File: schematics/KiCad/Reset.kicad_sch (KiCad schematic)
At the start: 15 parts, among them SW2 RESET, U13 74HC08, U14 74HC74, U14 DS1232, U15 DS1232, U2 74HC04, U9 74HC08, Y2 8MHz

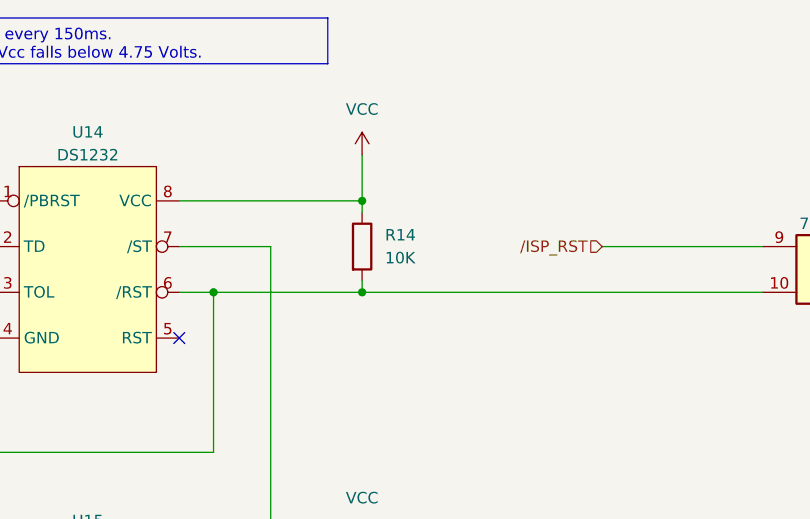
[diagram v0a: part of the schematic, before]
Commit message: Pull up ISP CLK by 10K ohm resistor.
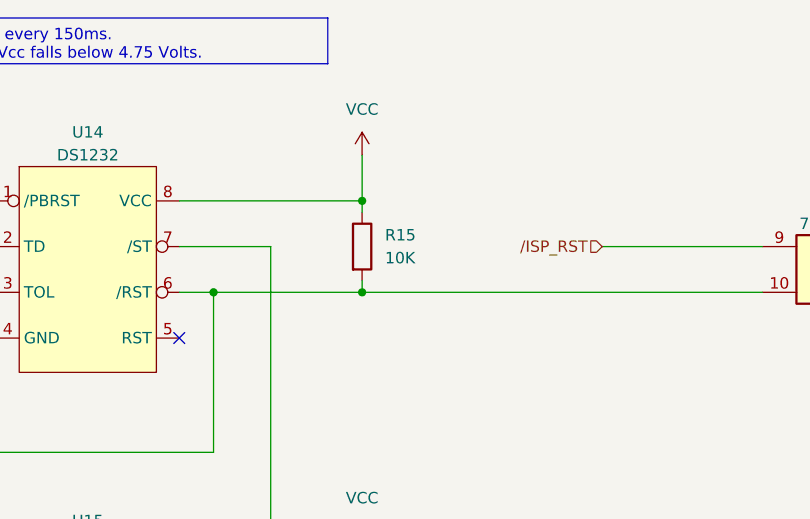
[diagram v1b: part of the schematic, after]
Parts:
- renumbered R14 to R15
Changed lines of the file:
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@@
   (title_block
     (title "Reset & Clock")
-    (date "2023-08-18")
+    (date "2023-08-27")
     (company "By 46nori")
   )
@@
         )
         (path "/8c0ff608-9e5b-458c-8fa7-b9973ff97e88/d23d98f9-7182-4fd3-8808-8c406ff55552"
-          (reference "R15") (unit 1)
+          (reference "R16") (unit 1)
         )
       )
@@
         )
         (path "/8c0ff608-9e5b-458c-8fa7-b9973ff97e88/d23d98f9-7182-4fd3-8808-8c406ff55552"
-          (reference "R16") (unit 1)
+          (reference "R17") (unit 1)
         )
       )
@@
   (symbol (lib_id "Device:R") (at 104.14 53.34 0) (unit 1)
     (in_bom yes) (on_board yes) (dnp no) (fields_autoplaced)
-    (property "Reference" "R14" (at 106.68 52.0699 0)
+    (property "Reference" "R15" (at 106.68 52.0699 0)
       (effects (font (size 1.27 1.27)) (justify left))
     )
@@
       (project "Z80ATmega128"
         (path "/8c0ff608-9e5b-458c-8fa7-b9973ff97e88/d23d98f9-7182-4fd3-8808-8c406ff55552"
-          (reference "R14") (unit 1)
+          (reference "R15") (unit 1)
         )
       )
@@
         )
         (path "/8c0ff608-9e5b-458c-8fa7-b9973ff97e88/d23d98f9-7182-4fd3-8808-8c406ff55552"
-          (reference "R17") (unit 1)
-        )
-      )
+          (reference "R18") (unit 1)
+        )
+      )

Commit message: Update schematics
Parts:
- U14, U15: footprint Package_DIP:DIP-8_W7.62mm -> Package_DIP:DIP-8_W7.62mm_Socket
- renumbered C10 to C?, C11 to C?, R1 to R?, R15 to R?, R16 to R?, TP3 to TP?, U9 to U11, U13 to U?, U2 to U?, U14 to U?, Y2 to Y?
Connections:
- net GND: now also C?.1; no longer C?.2
- net at C?.1, R?.2, U?.9: now also Y?.2; no longer Y?.1
- net at R?.1, R?.1, U?.8: now also C?.2, Y?.1; no longer C?.1, Y?.2

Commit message: Update for PCB design
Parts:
- removed TP?: 4MHz, TestPoint:TestPoint_Loop_D2.50mm_Drill1.0mm, symbol Connector:TestPoint
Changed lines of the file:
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@@
   (junction (at 45.72 101.6) (diameter 0) (color 0 0 0 0)
-  )
-  (junction (at 158.75 156.21) (diameter 0) (color 0 0 0 0)
   )
   (junction (at 45.72 58.42) (diameter 0) (color 0 0 0 0)
@@
     (stroke (width 0) (type default))
   )
-  (wire (pts (xy 158.75 156.21) (xy 172.72 156.21))
+  (wire (pts (xy 143.51 156.21) (xy 172.72 156.21))
     (stroke (width 0) (type default))
   )
@@
     (stroke (width 0) (type default))
   )
-  (wire (pts (xy 158.75 153.67) (xy 158.75 156.21))
-    (stroke (width 0) (type default))
-  )
   (wire (pts (xy 59.69 48.26) (xy 63.5 48.26))
     (stroke (width 0) (type default))
@@
   )
   (wire (pts (xy 45.72 162.56) (xy 45.72 158.75))
-    (stroke (width 0) (type default))
-  )
-  (wire (pts (xy 158.75 156.21) (xy 143.51 156.21))
     (stroke (width 0) (type default))
   )
@@
         )
       )
-    )
-  )
-  (symbol (lib_id "Connector:TestPoint") (at 158.75 153.67 0) (unit 1)
-    (in_bom yes) (on_board yes) (dnp no)
-    (property "Reference" "TP?" (at 161.29 149.0979 0)
-      (effects (font (size 1.27 1.27)) (justify left))
-    )
-    (property "Value" "4MHz" (at 161.29 151.13 0)
-      (effects (font (size 1.27 1.27)) (justify left))
-    )
-    (property "Footprint" "TestPoint:TestPoint_Loop_D2.50mm_Drill1.0mm" (at 163.83 153.67 0)
-      (effects (font (size 1.27 1.27)) hide)
-    )
-    (property "Datasheet" "~" (at 163.83 153.67 0)
-      (effects (font (size 1.27 1.27)) hide)
-    )
-    (pin "1")
-    (instances
-      (project "Z80ATmega128"
-        (path "/8c0ff608-9e5b-458c-8fa7-b9973ff97e88"
-          (reference "TP?") (unit 1)
-        )
-        (path "/8c0ff608-9e5b-458c-8fa7-b9973ff97e88/d23d98f9-7182-4fd3-8808-8c406ff55552"
-          (reference "TP3") (unit 1)
-        )
-      )

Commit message: Update document and BOM of schematics.
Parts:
- C? (x2): 部品名 (none) -> 22pF/50V 積層セラミックコンデンサ
- R15, R? (x3): 部品名 (none) -> 1/4Wカーボン抵抗
- SW2: 購入先(参考) (none) -> https://akizukidenshi.com/catalog/g/gP-03647/; 部品名 (none) -> タクトスイッチ
- U11, U?: 部品名 (none) -> 74HC08
- U14, U15: 購入先(参考) (none) -> https://akizukidenshi.com/catalog/g/gI-15313/; 部品名 (none) -> DS1232 マイクロモニターチップ
- U? (x2): 部品名 (none) -> 74HC04
- U?: 部品名 (none) -> 74HC74
- Y?: 購入先(参考) (none) -> https://akizukidenshi.com/catalog/g/gP-08667/; 部品名 (none) -> 8MHz 水晶発振子
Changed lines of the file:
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@@
+      (effects (font (size 1.27 1.27)) hide)
+    )
+    (property "購入先(参考)" "https://akizukidenshi.com/catalog/g/gP-08667/" (at 57.15 139.7 0)
+      (effects (font (size 1.27 1.27)) hide)
+    )
+    (property "部品名" "8MHz 水晶発振子" (at 57.15 139.7 0)
       (effects (font (size 1.27 1.27)) hide)
     )
@@
       (effects (font (size 1.27 1.27)) hide)
     )
+    (property "購入先(参考)" "" (at 45.72 166.37 0)
+      (effects (font (size 1.27 1.27)) hide)
+    )
+    (property "部品名" "22pF/50V 積層セラミックコンデンサ" (at 45.72 166.37 0)
+      (effects (font (size 1.27 1.27)) hide)
+    )
     (pin "1")
     (pin "2")
@@
       (effects (font (size 1.27 1.27)) hide)
     )
+    (property "購入先(参考)" "" (at 104.14 96.52 0)
+      (effects (font (size 1.27 1.27)) hide)
+    )
+    (property "部品名" "1/4Wカーボン抵抗" (at 104.14 96.52 0)
+      (effects (font (size 1.27 1.27)) hide)
+    )
     (pin "1")
     (pin "2")
@@
     )
     (property "Datasheet" "http://www.ti.com/lit/gpn/sn74HC08" (at 156.21 55.88 0)
+      (effects (font (size 1.27 1.27)) hide)
+    )
+    (property "購入先(参考)" "" (at 156.21 55.88 0)
+      (effects (font (size 1.27 1.27)) hide)
+    )
+    (property "部品名" "74HC08" (at 156.21 55.88 0)
       (effects (font (size 1.27 1.27)) hide)
     )
@@
       (effects (font (size 1.27 1.27)) hide)
     )
+    (property "購入先(参考)" "https://akizukidenshi.com/catalog/g/gI-15313/" (at 73.66 85.09 0)
+      (effects (font (size 1.27 1.27)) hide)
+    )
+    (property "部品名" "DS1232 マイクロモニターチップ" (at 73.66 85.09 0)
+      (effects (font (size 1.27 1.27)) hide)
+    )
     (pin "1")
     (pin "2")
@@
       (effects (font (size 1.27 1.27)) hide)
     )
+    (property "購入先(参考)" "" (at 57.15 158.75 0)
+      (effects (font (size 1.27 1.27)) hide)
+    )
+    (property "部品名" "1/4Wカーボン抵抗" (at 57.15 158.75 0)
+      (effects (font (size 1.27 1.27)) hide)
+    )
     (pin "1")
     (pin "2")
@@
     )
     (property "Datasheet" "~" (at 104.14 53.34 0)
+      (effects (font (size 1.27 1.27)) hide)
+    )
+    (property "購入先(参考)" "" (at 104.14 53.34 0)
+      (effects (font (size 1.27 1.27)) hide)
+    )
+    (property "部品名" "1/4Wカーボン抵抗" (at 104.14 53.34 0)
       (effects (font (size 1.27 1.27)) hide)
     )
@@
       (effects (font (size 1.27 1.27)) hide)
     )
-    (property "Datasheet" "https://assets.nexperia.com/documents/data-sheet/74HC_HCT04.pdf" (at 57.15 149.86 0)
+    (property "Datasheet" "http://www.ti.com/lit/gpn/sn74HC04" (at 57.15 149.86 0)
+      (effects (font (size 1.27 1.27)) hide)
+    )
+    (property "購入先(参考)" "" (at 57.15 149.86 0)
+      (effects (font (size 1.27 1.27)) hide)
+    )
+    (property "部品名" "74HC04" (at 57.15 149.86 0)
       (effects (font (size 1.27 1.27)) hide)
     )
@@
       (effects (font (size 1.27 1.27)) hide)
     )
+    (property "購入先(参考)" "" (at 68.58 166.37 0)
+      (effects (font (size 1.27 1.27)) hide)
+    )
+    (property "部品名" "22pF/50V 積層セラミックコンデンサ" (at 68.58 166.37 0)
+      (effects (font (size 1.27 1.27)) hide)
+    )
     (pin "1")
     (pin "2")
@@
       (effects (font (size 1.27 1.27)) hide)
     )
-    (property "Datasheet" "74xx/74hc_hct74.pdf" (at 118.11 158.75 0)
+    (property "Datasheet" "http://www.ti.com/lit/gpn/sn74HC74" (at 118.11 158.75 0)
+      (effects (font (size 1.27 1.27)) hide)
+    )
+    (property "購入先(参考)" "" (at 118.11 158.75 0)
+      (effects (font (size 1.27 1.27)) hide)
+    )
+    (property "部品名" "74HC74" (at 118.11 158.75 0)
       (effects (font (size 1.27 1.27)) hide)
     )
@@
       (effects (font (size 1.27 1.27)) hide)
     )
-    (property "Datasheet" "https://assets.nexperia.com/documents/data-sheet/74HC_HCT04.pdf" (at 95.25 158.75 0)
+    (property "Datasheet" "http://www.ti.com/lit/gpn/sn74HC04" (at 95.25 158.75 0)
+      (effects (font (size 1.27 1.27)) hide)
+    )
+    (property "購入先(参考)" "" (at 95.25 158.75 0)
+      (effects (font (size 1.27 1.27)) hide)
+    )
+    (property "部品名" "74HC04" (at 95.25 158.75 0)
       (effects (font (size 1.27 1.27)) hide)
     )
@@
       (effects (font (size 1.27 1.27)) hide)
     )
-    (property "Datasheet" "http://www.ti.com/lit/gpn/sn74LS08" (at 156.21 104.14 0)
+    (property "Datasheet" "http://www.ti.com/lit/gpn/sn74HC08" (at 156.21 104.14 0)
+      (effects (font (size 1.27 1.27)) hide)
+    )
+    (property "購入先(参考)" "" (at 156.21 104.14 0)
+      (effects (font (size 1.27 1.27)) hide)
+    )
+    (property "部品名" "74HC08" (at 156.21 104.14 0)
       (effects (font (size 1.27 1.27)) hide)
     )
@@
       (effects (font (size 1.27 1.27)) hide)
     )
-    (property "Datasheet" "~" (at 54.61 43.18 0)
+    (property "Datasheet" "https://akizukidenshi.com/download/ds/cosland/ts-0606_20200714.pdf" (at 54.61 43.18 0)
+      (effects (font (size 1.27 1.27)) hide)
+    )
+    (property "購入先(参考)" "https://akizukidenshi.com/catalog/g/gP-03647/" (at 54.61 48.26 0)
+      (effects (font (size 1.27 1.27)) hide)
+    )
+    (property "部品名" "タクトスイッチ" (at 54.61 48.26 0)
       (effects (font (size 1.27 1.27)) hide)
     )
@@
     )
     (property "Datasheet" "https://akizukidenshi.com/download/ds/htc/ds1232.pdf" (at 73.66 34.29 0)
+      (effects (font (size 1.27 1.27)) hide)
+    )
+    (property "購入先(参考)" "https://akizukidenshi.com/catalog/g/gI-15313/" (at 73.66 41.91 0)
+      (effects (font (size 1.27 1.27)) hide)
+    )
+    (property "部品名" "DS1232 マイクロモニターチップ" (at 73.66 41.91 0)
       (effects (font (size 1.27 1.27)) hide)
     )
@@
       (effects (font (size 1.27 1.27)) hide)
     )
+    (property "購入先(参考)" "" (at 80.01 158.75 0)
+      (effects (font (size 1.27 1.27)) hide)
+    )
+    (property "部品名" "1/4Wカーボン抵抗" (at 80.01 158.75 0)
+      (effects (font (size 1.27 1.27)) hide)
+    )
